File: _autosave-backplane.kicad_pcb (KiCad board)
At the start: 4 copper layers, 110 x 90 mm, 57 parts, among them IC1 SiC437AED-T1-GE3, J1 46010-0622, J2 46010-0622, J4 212520-1006, J5 XT60PW-F

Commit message: resolving more violations
connections etc
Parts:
- moved C39 0.78 mm to (137.8, 134.0)
- moved R21 0.70 mm to (124.0, 128.0)
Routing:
- net RBUS_uC_V: track 3.11 -> 3.82 mm
- net /buckC/FB: track 4.00 -> 4.71 mm
- added copper zone on F.Cu, net RBUS_uC_V
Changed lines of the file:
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@@
 	(footprint "Resistor_SMD:R_0402_1005Metric"
 		(layer "F.Cu")
-		(at 121.905661 128.48 180)
+		(at 121.905661 128.5 180)
 		(descr "Resistor SMD 0402 (1005 Metric), square (rectangular) end terminal, IPC_7351 nominal, (Body size source: IPC-SM-782 page 72, https://www.pcb-3d.com/wordpress/wp-content/uploads/ipc-sm-782a_amendment_1_and_2.pdf), generated with kicad-footprint-generator")
 		(tags "resistor")
 		(property "Reference" "R22"
-			(at -0.094339 -2.02 90)
+			(at -0.094339 -2 90)
 			(layer "F.SilkS")
 			(effects
@@
 	(footprint "Capacitor_SMD:C_0603_1608Metric"
 		(layer "F.Cu")
-		(at 137.775 133.225 90)
+		(at 137.775 134 90)
 		(descr "Capacitor SMD 0603 (1608 Metric), square (rectangular) end terminal, IPC_7351 nominal, (Body size source: IPC-SM-782 page 76, https://www.pcb-3d.com/wordpress/wp-content/uploads/ipc-sm-782a_amendment_1_and_2.pdf), generated with kicad-footprint-generator")
 		(tags "capacitor")
@@
 	(footprint "Resistor_SMD:R_0402_1005Metric"
 		(layer "F.Cu")
-		(at 123.295094 128.027312 90)
+		(at 124 128.027312 90)
 		(descr "Resistor SMD 0402 (1005 Metric), square (rectangular) end terminal, IPC_7351 nominal, (Body size source: IPC-SM-782 page 72, https://www.pcb-3d.com/wordpress/wp-content/uploads/ipc-sm-782a_amendment_1_and_2.pdf), generated with kicad-footprint-generator")
 		(tags "resistor")
 		(property "Reference" "R21"
-			(at 0 1.204906 -90)
+			(at 0.027312 1.5 -90)
 			(layer "F.SilkS")
 			(effects
@@
 	(segment
 		(start 122.472973 128.537312)
-		(end 122.415661 128.48)
-		(width 0.25)
-		(layer "F.Cu")
-		(net 11)
-	)
-	(segment
-		(start 123.295094 128.537312)
-		(end 122.472973 128.537312)
+		(end 120.594222 126.658561)
 		(width 0.25)
 		(layer "F.Cu")
@@
 	(segment
 		(start 120.594222 126.658561)
-		(end 122.415661 128.48)
+		(end 120.069962 126.658561)
 		(width 0.25)
 		(layer "F.Cu")
@@
 	)
 	(segment
-		(start 120.069962 126.658561)
-		(end 120.594222 126.658561)
+		(start 124 128.537312)
+		(end 122.472973 128.537312)
 		(width 0.25)
 		(layer "F.Cu")
@@
 	)
 	(segment
-		(start 121.974343 126.196561)
-		(end 123.295094 127.517312)
+		(start 122.679249 126.196561)
+		(end 124 127.517312)
 		(width 0.25)
 		(layer "F.Cu")
@@
 	)
 	(segment
-		(start 121.803439 126.196561)
-		(end 120.731962 126.196561)
-		(width 0.25)
-		(layer "F.Cu")
-		(net 22)
-	)
-	(segment
-		(start 121.803439 126.196561)
-		(end 121.974343 126.196561)
+		(start 120.731962 126.196561)
+		(end 122.679249 126.196561)
 		(width 0.25)
 		(layer "F.Cu")
@@
 	)
 	(zone
-		(net 0)
-		(net_name "")
+		(net 22)
+		(net_name "RBUS_uC_V")
 		(layer "F.Cu")
 		(hatch edge 0.5)
+		(priority 3)
 		(connect_pads
 			(clearance 0)
@@
 		(min_thickness 0.25)
 		(filled_areas_thickness no)
-		(keepout
-			(tracks not_allowed)
-			(vias not_allowed)
-			(pads not_allowed)
-			(copperpour allowed)
-			(footprints allowed)
-		)
-		(fill
+		(fill yes
 			(thermal_gap 0.5)
 			(thermal_bridge_width 0.5)
@@
 		(polygon
 			(pts
-				(xy 106 116.84998) (xy 98.293282 116.84998) (xy 98.244014 139.193289) (xy 105.9541 139.189812)
+				(xy 144.5 134) (xy 144.5 141) (xy 98.5 141) (xy 98.5 134)
 			)
 		)
 	)
 	(zone
-		(net 0)
-		(net_name "")
+		(net 22)
+		(net_name "RBUS_uC_V")
 		(layer "F.Cu")
 		(hatch edge 0.5)
+		(priority 3)
 		(connect_pads
 			(clearance 0)
@@
 		(min_thickness 0.25)
 		(filled_areas_thickness no)
-		(keepout
-			(tracks not_allowed)
-			(vias not_allowed)
-			(pads not_allowed)
-			(copperpour allowed)
-			(footprints allowed)
-		)
-		(fill
+		(fill yes
 			(thermal_gap 0.5)
 			(thermal_bridge_width 0.5)
@@
 		(polygon
 			(pts
-				(xy 143.851182 139.133011) (xy 143.851182 133.426293) (xy 98.754924 133.647059) (xy 98.758401 139.357145)
+				(xy 105.5 141) (xy 98.217857 141.042101) (xy 98.217857 116.819394) (xy 105.5 116.777293)
 			)
 		)

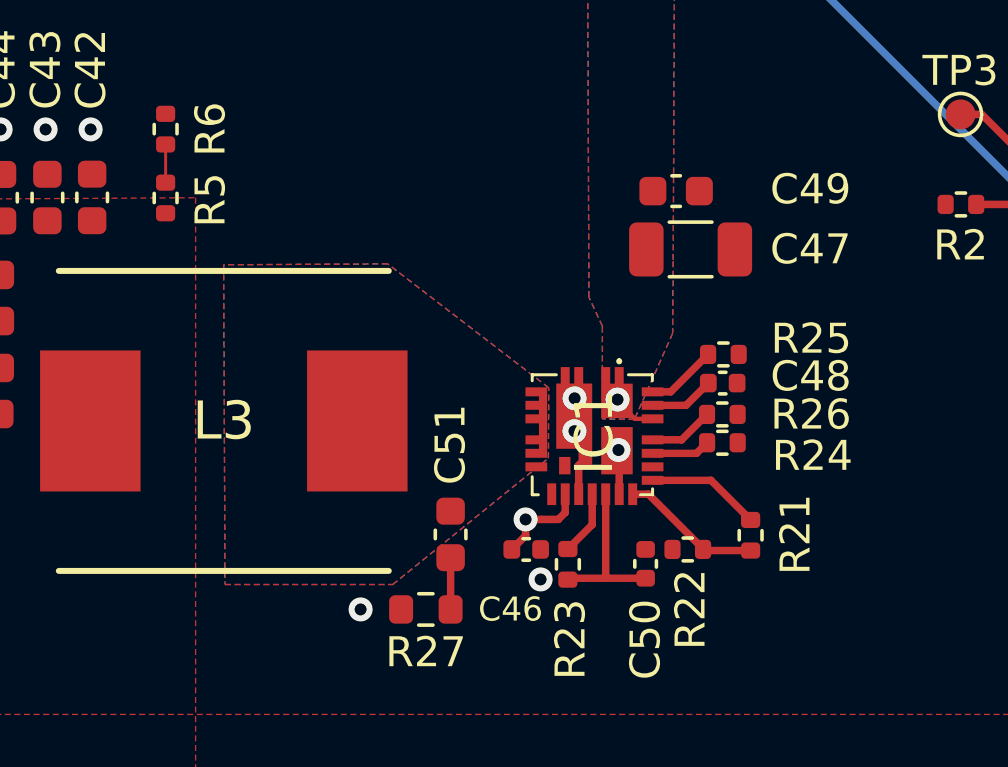
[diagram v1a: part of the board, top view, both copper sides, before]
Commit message: 10 more to go
DRC reduction
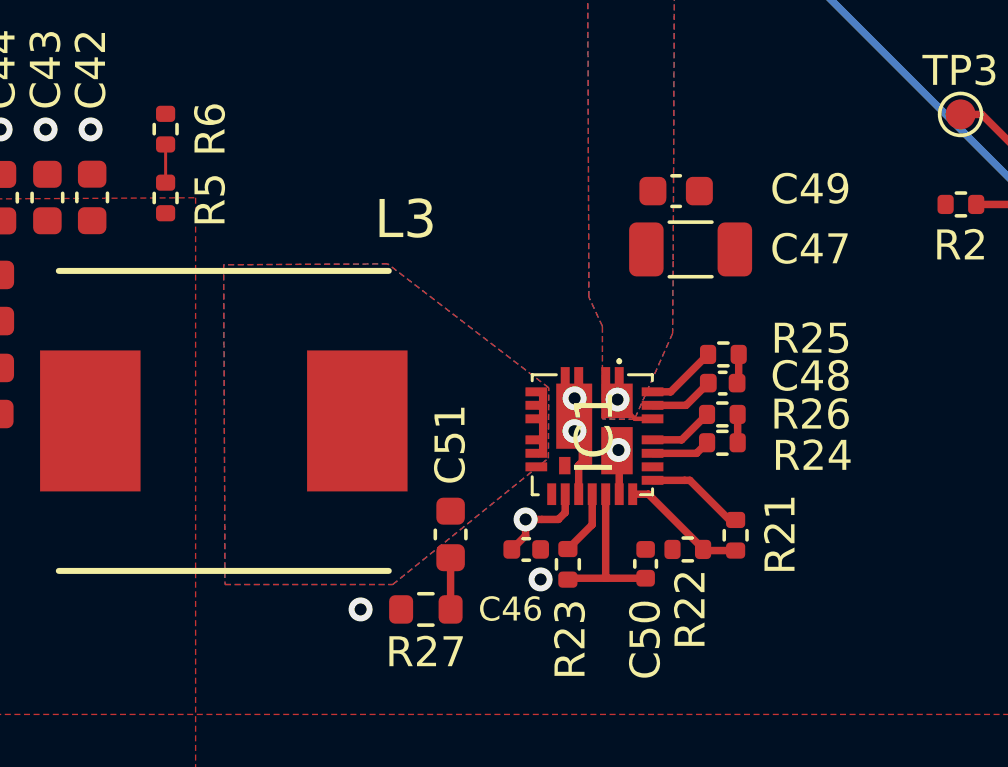
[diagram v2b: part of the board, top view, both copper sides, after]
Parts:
- moved R21 0.50 mm to (123.5, 128.0)
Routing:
- net Net-(C48-Pad2): track 0.00 -> 0.98 mm
- net /buckC/Vdd: track 5.41 -> 6.36 mm
- net /buckC/FB: track 4.71 -> 4.00 mm
- net RBUS_uC_V: track 3.82 -> 3.13 mm
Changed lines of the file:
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@@
 		(tags "Inductor")
 		(property "Reference" "L3"
-			(at 0 0 0)
+			(at 6.059832 -6.716397 0)
 			(layer "F.SilkS")
 			(effects
@@
 	(footprint "Resistor_SMD:R_0402_1005Metric"
 		(layer "F.Cu")
-		(at 124 128.027312 90)
+		(at 123.5 128.027312 90)
 		(descr "Resistor SMD 0402 (1005 Metric), square (rectangular) end terminal, IPC_7351 nominal, (Body size source: IPC-SM-782 page 72, https://www.pcb-3d.com/wordpress/wp-content/uploads/ipc-sm-782a_amendment_1_and_2.pdf), generated with kicad-footprint-generator")
 		(tags "resistor")
@@
 	)
 	(segment
+		(start 123.602837 122)
+		(end 123.602837 122.902478)
+		(width 0.25)
+		(layer "F.Cu")
+		(net 7)
+	)
+	(segment
+		(start 123.602837 122.902478)
+		(end 123.54975 122.955565)
+		(width 0.25)
+		(layer "F.Cu")
+		(net 7)
+	)
+	(segment
 		(start 119.169962 129.459173)
 		(end 119.170789 129.46)
@@
 	)
 	(segment
+		(start 123.567962 124.943322)
+		(end 123.568944 124.944304)
+		(width 0.25)
+		(layer "F.Cu")
+		(net 9)
+	)
+	(segment
 		(start 119.170789 129.46)
 		(end 117.955511 129.46)
@@
 	)
 	(segment
+		(start 123.567962 124)
+		(end 123.567962 124.943322)
+		(width 0.25)
+		(layer "F.Cu")
+		(net 9)
+	)
+	(segment
 		(start 119.169962 126.658561)
 		(end 119.169962 129.459173)
@@
 	(segment
 		(start 122.472973 128.537312)
-		(end 120.594222 126.658561)
+		(end 122.415661 128.48)
+		(width 0.25)
+		(layer "F.Cu")
+		(net 11)
+	)
+	(segment
+		(start 123.295094 128.537312)
+		(end 122.472973 128.537312)
 		(width 0.25)
 		(layer "F.Cu")
@@
 	(segment
 		(start 120.594222 126.658561)
-		(end 120.069962 126.658561)
+		(end 122.415661 128.48)
 		(width 0.25)
 		(layer "F.Cu")
@@
 	)
 	(segment
-		(start 124 128.537312)
-		(end 122.472973 128.537312)
+		(start 120.069962 126.658561)
+		(end 120.594222 126.658561)
 		(width 0.25)
 		(layer "F.Cu")
@@
 	)
 	(segment
-		(start 122.679249 126.196561)
-		(end 124 127.517312)
+		(start 121.974343 126.196561)
+		(end 123.295094 127.517312)
 		(width 0.25)
 		(layer "F.Cu")
@@
 	)
 	(segment
-		(start 120.731962 126.196561)
-		(end 122.679249 126.196561)
+		(start 121.803439 126.196561)
+		(end 120.731962 126.196561)
+		(width 0.25)
+		(layer "F.Cu")
+		(net 22)
+	)
+	(segment
+		(start 121.803439 126.196561)
+		(end 121.974343 126.196561)
+		(width 0.25)
+		(layer "F.Cu")
+		(net 22)
+	)
+	(segment
+		(start 123.517312 127.5)
+		(end 123.5 127.517312)
 		(width 0.25)
 		(layer "F.Cu")
@@
 		(priority 1)
 		(connect_pads yes
-			(clearance 0.5)
+			(clearance 0.254)
 		)
-		(min_thickness 0.25)
+		(min_thickness 0.254)
 		(filled_areas_thickness no)
 		(fill yes
